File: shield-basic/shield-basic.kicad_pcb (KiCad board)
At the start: 2 copper layers, 0 parts

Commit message: Place the components in the Board. Change some footprint because kicad will remove the library.
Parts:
- added 1pin: VAL**, Connect:1pin, F.Cu at (191.0, 50.0)
- added 1pin: VAL**, Connect:1pin, F.Cu at (132.0, 50.0)
- added 1pin: VAL**, Connect:1pin, F.Cu at (191.0, 117.0)
- added 1pin: VAL**, Connect:1pin, F.Cu at (132.0, 117.0)
- added C1: 18n, Capacitors_SMD:C_0805, F.Cu at (141.0, 57.0)
- added C10: 2.2u, Capacitors_SMD:C_0805, F.Cu at (180.0, 80.0)
- added C11: 10n, Capacitors_SMD:C_0805, F.Cu at (176.0, 88.0)
- added C12: 220u, Capacitors_SMD:c_elec_6.3x7.7, F.Cu at (169.0, 90.0)
- added C13: 100n, Capacitors_SMD:C_0805, F.Cu at (180.0, 88.0)
- added C2: 100nF, Capacitors_SMD:C_0805, F.Cu at (159.0, 57.0)
- added C3: 18n, Capacitors_SMD:C_0805, F.Cu at (165.0, 57.0)
- added C4: 100 nF, Capacitors_SMD:C_0805, F.Cu at (159.0, 68.0)
- added C5: 3.3 uF, Capacitors_SMD:C_0805, F.Cu at (162.0, 68.0)
- added C6: 100 nF, Capacitors_SMD:C_0805, F.Cu at (159.0, 80.0)
- added C7: 47n, Capacitors_SMD:C_0805, F.Cu at (144.0, 88.0)
- added C8: 10 uF, Capacitors_SMD:C_0805, F.Cu at (147.0, 88.0)
- added C9: 100n, Capacitors_SMD:C_0805, F.Cu at (176.0, 80.0)
- added CON1: SD_Card, Connect:SD_Card_Receptacle, B.Cu at (132.0, 69.0)
- added D1: LED_RGB_A, Dreamster:rgb_led_plcc6, F.Cu at (161.0, 112.0)
- added IC1: DRV8833, Housings_SSOP:TSSOP-16_4.4x5mm_Pitch0.65mm, F.Cu at (169.0, 81.0)
- added L1: 1 uH, Capacitors_SMD:C_0805, F.Cu at (156.0, 57.0)
- added L2: 1 uH, Capacitors_SMD:C_0805, F.Cu at (156.0, 68.0)
- added L3: 1 uH, Capacitors_SMD:C_0805, F.Cu at (156.0, 80.0)
- added P1: CONN_01X04, Socket_Strips:Socket_Strip_Straight_1x04, F.Cu at (193.0, 105.0)
- added P2: CONN_01X04, Socket_Strips:Socket_Strip_Straight_1x04, F.Cu at (193.0, 63.0)
- added P3: CONN_01X04, Socket_Strips:Socket_Strip_Straight_1x04, F.Cu at (161.5, 119.5)
- added P4: CONN_01X04, Socket_Strips:Socket_Strip_Straight_1x04, F.Cu at (130.0, 105.0)
- added P5: CONN_01X04, Socket_Strips:Socket_Strip_Straight_1x04, F.Cu at (130.0, 63.0)
- added P6: CONN_01X02, Socket_Strips:Socket_Strip_Straight_1x02, F.Cu at (184.0, 109.0)
- added P7: CONN_01X02, Socket_Strips:Socket_Strip_Straight_1x02, F.Cu at (178.0, 109.0)
- added P8: CONN_01X06, Socket_Strips:Socket_Strip_Straight_1x06, F.Cu at (178.0, 118.0)
- added P9: speaker, Socket_Strips:Socket_Strip_Straight_1x02, F.Cu at (138.0, 112.0)
- added Q1: PNP, Transistors_SMD:sot23, F.Cu at (174.0, 54.0)
- added Q2: NPN, Transistors_SMD:sot23, F.Cu at (157.0, 103.0)
- added R1: 10k, Resistors_SMD:R_0805, F.Cu at (169.0, 114.0)
- added R10: 100, Resistors_SMD:R_0805, F.Cu at (193.0, 71.0)
- added R11: 10k, Resistors_SMD:R_0805, F.Cu at (192.0, 96.0)
- added R12: 10k, Resistors_SMD:R_0805, F.Cu at (161.0, 103.0)
- added R2: 10k, Resistors_SMD:R_0805, F.Cu at (169.0, 111.0)
- added R3: 10k, Resistors_SMD:R_0805, F.Cu at (169.0, 108.0)
- added R4: 2.2k, Resistors_SMD:R_0805, F.Cu at (144.0, 57.0)
- added R5: 2.2k, Resistors_SMD:R_0805, F.Cu at (162.0, 57.0)
- added R6: 10, Resistors_SMD:R_0805, F.Cu at (144.0, 80.0)
- added R7: 100, Resistors_SMD:R_0805, F.Cu at (130.0, 71.0)
- added R8: 100, Resistors_SMD:R_0805, F.Cu at (174.0, 58.0)
- added R9: 10k, Resistors_SMD:R_0805, F.Cu at (131.0, 96.0)
- added RV1: 10k, SMD_Packages:POT_SMD, F.Cu at (147.0, 112.0)
- added RV2: POT, SMD_Packages:POT_SMD, F.Cu at (131.0, 91.0)
- added RV3: POT, SMD_Packages:POT_SMD, F.Cu at (192.0, 91.0)
- added U1: TL082, Housings_SOIC:SOIC-8_3.9x4.9mm_Pitch1.27mm, F.Cu at (150.0, 58.0)
- added U19: TL082, Housings_SOIC:SOIC-8_3.9x4.9mm_Pitch1.27mm, F.Cu at (150.0, 69.0)
- added U2: LM386, Housings_SSOP:MSOP-8_3x3mm_Pitch0.65mm, F.Cu at (150.0, 80.0)
- added U3: TCRT1000, Socket_Strips:Socket_Strip_Angled_1x04, F.Cu at (130.0, 79.0)
- added U4: TCRT1000, Socket_Strips:Socket_Strip_Angled_1x04, F.Cu at (193.0, 79.0)
- added U5: ARDUINO_SHIELD, Dreamster:arduino_shield, F.Cu at (188.0, 47.0)
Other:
- board outline added: 67 x 75 mm

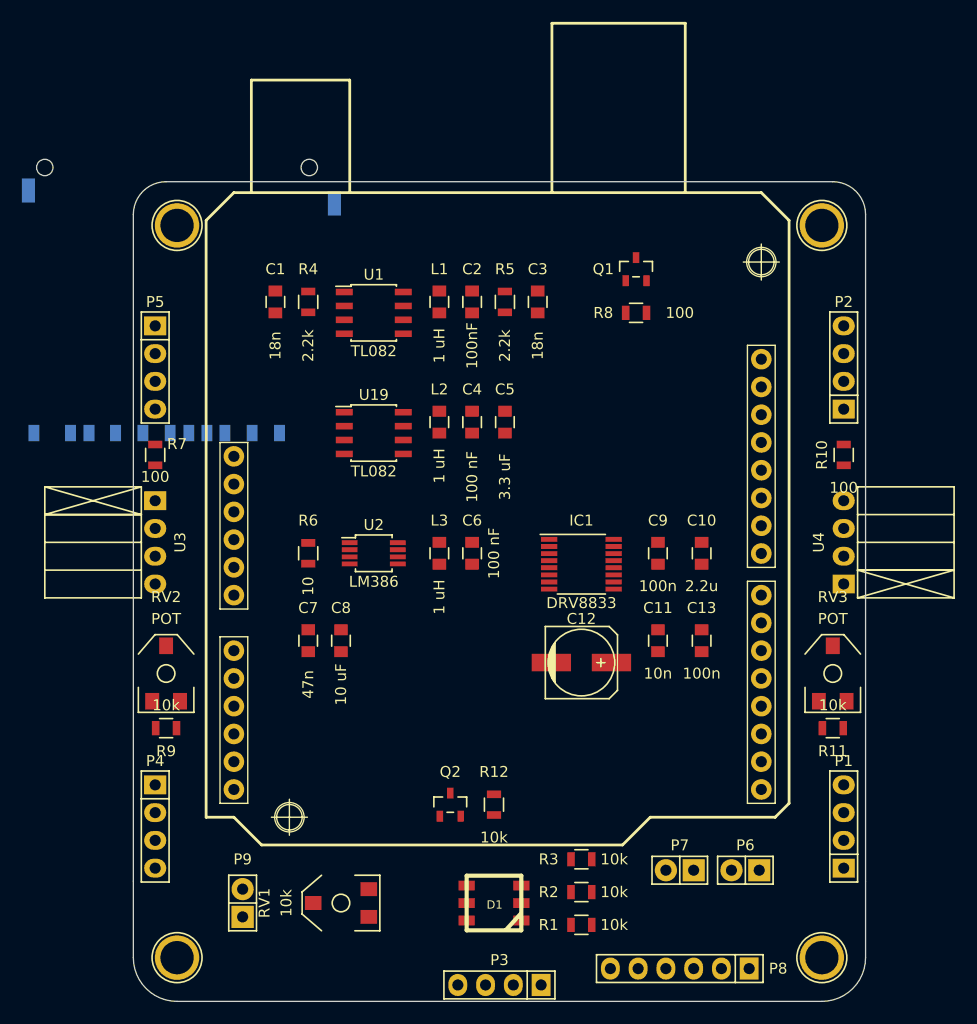
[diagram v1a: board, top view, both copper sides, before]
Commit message: Change the board size
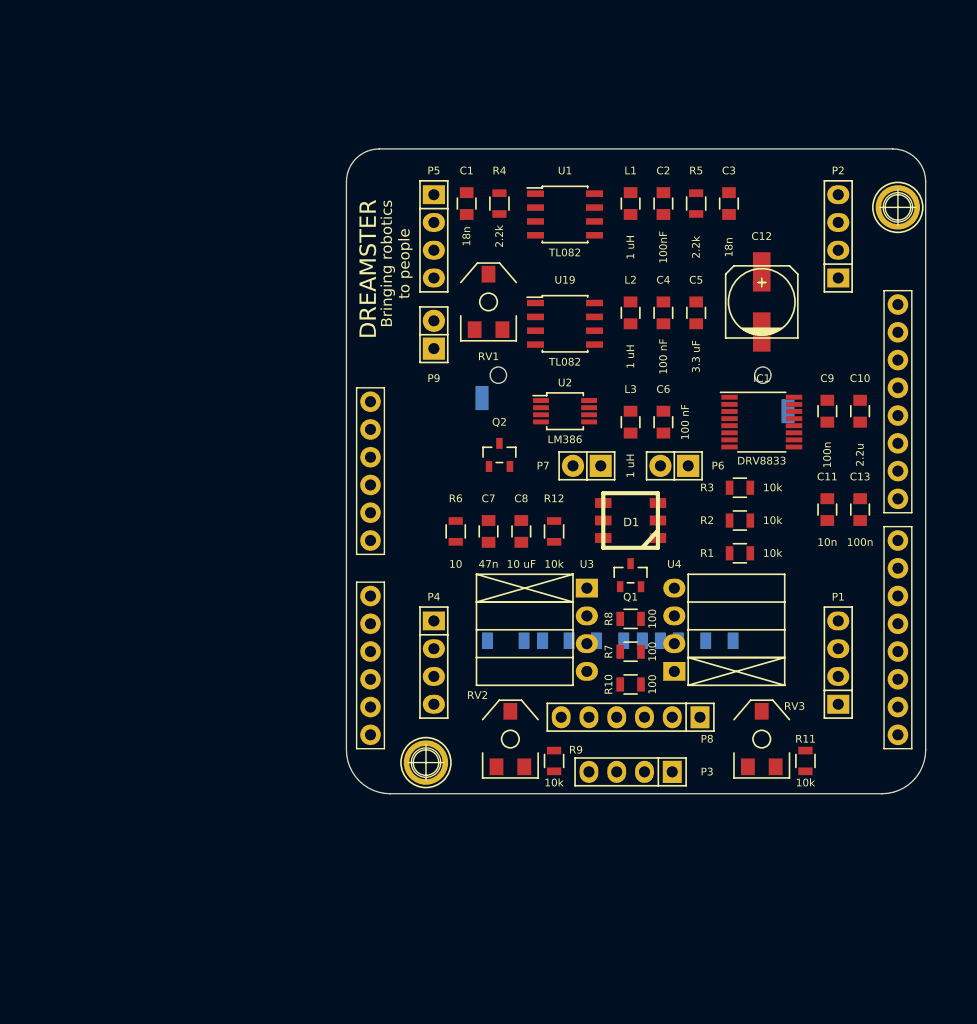
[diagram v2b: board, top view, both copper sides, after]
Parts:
- removed the 1pin at (191.0, 50.0)
- removed the 1pin at (132.0, 117.0)
- moved 1pin 66.0 mm to (197.9, 48.4)
- moved RV1 56.6 mm to (160.5, 57.0), turned to 0 degrees
- moved P9 54.9 mm to (155.5, 60.0)
- moved R7 47.1 mm to (173.5, 89.0), turned to 0 degrees
- moved CON1 45.6 mm to (173.5, 88.0)
- moved 1pin 40.4 mm to (154.8, 99.2)
- moved U3 40.3 mm to (169.5, 87.0)
- moved P7 38.0 mm to (169.5, 72.0)
- moved P6 37.6 mm to (177.5, 72.0)
- moved D1 37.2 mm to (173.5, 77.0)
- moved R1 37.0 mm to (183.5, 80.0)
- moved R2 37.0 mm to (183.5, 77.0)
- moved R3 37.0 mm to (183.5, 74.0)
- moved C12 36.9 mm to (185.5, 57.0), turned to 90 degrees
- moved R9 35.6 mm to (166.5, 99.0), turned to 270 degrees
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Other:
- board size 67 x 75 mm -> 53 x 59 mm
- board text added: "Bringing robotics to people"
- board text added: "DREAMSTER"

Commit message: Added reset buttom.
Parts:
- added C14: 100n, Capacitors_SMD:C_0805, F.Cu at (164.0, 68.0)
- added C15: 100n, Capacitors_SMD:C_0805, F.Cu at (161.0, 68.0)
- added D2: CD1206-S01575, Capacitors_SMD:C_1206, F.Cu at (150.5, 62.0)
- added R13: 10k, Resistors_SMD:R_0805, F.Cu at (154.0, 75.5)
- added SW1: SW_PUSH, Discret:SW_PUSH_SMALL, F.Cu at (155.5, 68.5)
- C2: value 100nF -> 100n
- C4, C6: value 100 nF -> 100n
- C5: value 3.3 uF -> 3.3u
- C8: value 10 uF -> 10u
- L1, L2, L3: value 1 uH -> 1u
- moved Q2 12.5 mm to (154.0, 81.0)
- moved U2 1.50 mm to (169.0, 67.0)
- moved C6 1.41 mm to (177.5, 67.0)
- moved L3 1.41 mm to (174.5, 67.0)
- moved C2 1.00 mm to (177.5, 48.0)
- moved C3 1.00 mm to (183.5, 48.0)
- moved C4 1.00 mm to (177.5, 58.0)
- moved C5 1.00 mm to (180.5, 58.0)
- moved L1 1.00 mm to (174.5, 48.0)
- moved L2 1.00 mm to (174.5, 58.0)
- moved R3 1.00 mm to (183.5, 75.0)
- moved R5 1.00 mm to (180.5, 48.0)
- moved U3 1.00 mm to (168.5, 87.0)
- moved U4 1.00 mm to (178.5, 87.0)
- moved C1 0.50 mm to (159.0, 48.0)
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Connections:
- U5 pad RES: (no net) -> /RESET

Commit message: Correct HCS04 sensor position.
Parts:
- turned P3 to 180 degrees
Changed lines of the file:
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@@
   )
   (module Socket_Strips:Socket_Strip_Straight_1x04 (layer F.Cu)
-    (at 173.5 100)
+    (at 173.5 100 180)
     (descr "Through hole socket strip")
     (tags "socket strip")
-    (fp_text reference P3 (at 6.5 0) (layer F.SilkS)
+    (fp_text reference P3 (at 4.5 2 180) (layer F.SilkS)
       (effects (font (size 0.7 0.7) (thickness 0.125)))
     )
-    (fp_text value CONN_01X04 (at 0 0) (layer F.SilkS) hide
+    (fp_text value CONN_01X04 (at 0 0 180) (layer F.SilkS) hide
       (effects (font (size 0.7 0.7) (thickness 0.125)))
     )
@@
     (fp_line (start 5.08 -1.27) (end 5.08 1.27) (layer F.SilkS) (width 0.15))
     (fp_line (start 5.08 1.27) (end 2.54 1.27) (layer F.SilkS) (width 0.15))
-    (pad 1 thru_hole rect (at 3.81 0 180) (size 1.7272 2.032) (drill 1.016) (layers *.Cu *.Mask F.SilkS)
+    (pad 1 thru_hole rect (at 3.81 0) (size 1.7272 2.032) (drill 1.016) (layers *.Cu *.Mask F.SilkS)
       (net 9 +5VD))
-    (pad 2 thru_hole oval (at 1.27 0 180) (size 1.7272 2.032) (drill 1.016) (layers *.Cu *.Mask F.SilkS)
+    (pad 2 thru_hole oval (at 1.27 0) (size 1.7272 2.032) (drill 1.016) (layers *.Cu *.Mask F.SilkS)
       (net 23 /TRG_A))
-    (pad 3 thru_hole oval (at -1.27 0 180) (size 1.7272 2.032) (drill 1.016) (layers *.Cu *.Mask F.SilkS)
+    (pad 3 thru_hole oval (at -1.27 0) (size 1.7272 2.032) (drill 1.016) (layers *.Cu *.Mask F.SilkS)
       (net 24 /ECHO_A))
-    (pad 4 thru_hole oval (at -3.81 0 180) (size 1.7272 2.032) (drill 1.016) (layers *.Cu *.Mask F.SilkS)
+    (pad 4 thru_hole oval (at -3.81 0) (size 1.7272 2.032) (drill 1.016) (layers *.Cu *.Mask F.SilkS)
       (net 2 GND))
     (model Socket_Strips/Socket_Strip_Straight_1x04.wrl

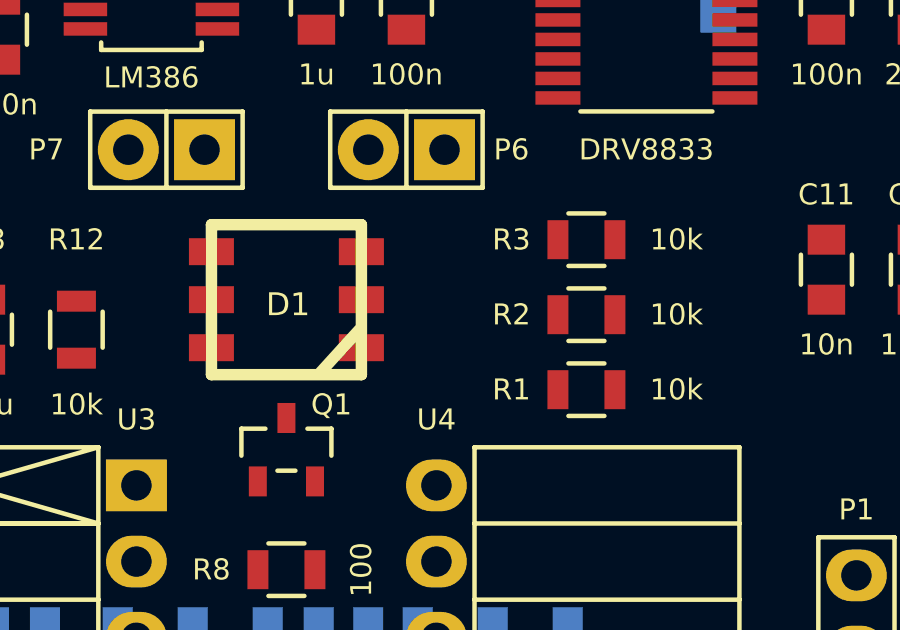
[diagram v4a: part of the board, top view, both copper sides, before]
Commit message: Correct LED RGB position.
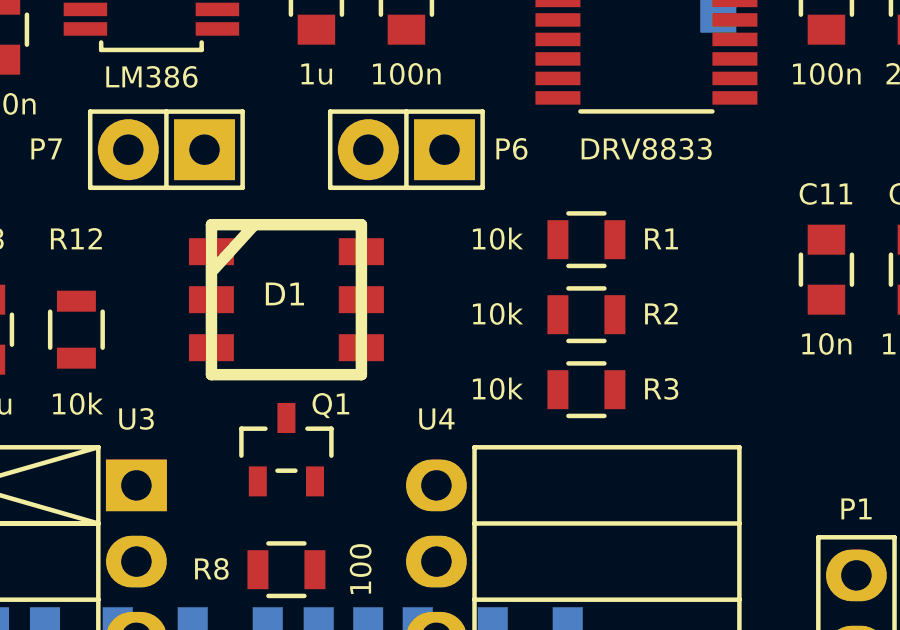
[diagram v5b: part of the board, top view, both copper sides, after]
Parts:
- moved R1 5.00 mm to (183.5, 75.0), turned to 180 degrees
- moved R3 5.00 mm to (183.5, 80.0), turned to 180 degrees
- turned D1 to 180 degrees
- turned R2 to 180 degrees
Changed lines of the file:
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@@
     (links 141)
     (no_connects 141)
-    (area 147.449999 42.949999 200.550001 102.050001)
+    (area 143.790048 41.496 201.004 105.299833)
     (thickness 1.6)
     (drawings 10)
@@
     (add_net "Net-(RV1-Pad2)")
   )
+  (module Dreamster:rgb_led_plcc6 (layer F.Cu)
+    (at 173.5 77 180)
+    (fp_text reference D1 (at 0.05334 0.16256 180) (layer F.SilkS)
+      (effects (font (size 0.762 0.762) (thickness 0.127)))
+    )
+    (fp_text value LED_RGB_A (at 0 3.429 180) (layer F.SilkS) hide
+      (effects (font (size 0.762 0.762) (thickness 0.127)))
+    )
+    (fp_line (start 1.143 2.413) (end 2.413 1.016) (layer F.SilkS) (width 0.381))
+    (fp_line (start -2.49936 2.49936) (end -2.49936 -2.49936) (layer F.SilkS) (width 0.381))
+    (fp_line (start -2.49936 -2.49936) (end 2.49936 -2.49936) (layer F.SilkS) (width 0.381))
+    (fp_line (start 2.49936 -2.49936) (end 2.49936 2.49936) (layer F.SilkS) (width 0.381))
+    (fp_line (start 2.49936 2.49936) (end -2.49936 2.49936) (layer F.SilkS) (width 0.381))
+    (pad 4 smd rect (at -2.49936 -1.6002 270) (size 0.89916 1.50114) (layers F.Cu F.Paste F.Mask)
+      (net 18 "Net-(D1-Pad4)"))
+    (pad 5 smd rect (at -2.49936 0 270) (size 0.89916 1.50114) (layers F.Cu F.Paste F.Mask)
+      (net 16 "Net-(D1-Pad5)"))
+    (pad 6 smd rect (at -2.49936 1.6002 270) (size 0.89916 1.50114) (layers F.Cu F.Paste F.Mask)
+      (net 17 "Net-(D1-Pad6)"))
+    (pad 1 smd rect (at 2.49936 1.6002 270) (size 0.89916 1.50114) (layers F.Cu F.Paste F.Mask)
+      (net 15 "Net-(D1-Pad1)"))
+    (pad 2 smd rect (at 2.49936 0 270) (size 0.89916 1.50114) (layers F.Cu F.Paste F.Mask)
+      (net 15 "Net-(D1-Pad1)"))
+    (pad 3 smd rect (at 2.49936 -1.6002 270) (size 0.89916 1.50114) (layers F.Cu F.Paste F.Mask)
+      (net 15 "Net-(D1-Pad1)"))
+  )
   (module Connect:1pin (layer F.Cu)
     (at 154.775 99.15)
@@
     (pad "" np_thru_hole circle (at -12.1 -24.3) (size 1.5 1.5) (drill 1.5) (layers *.Cu *.Mask B.SilkS))
   )
-  (module Dreamster:rgb_led_plcc6 (layer F.Cu)
-    (at 173.5 77)
-    (fp_text reference D1 (at 0.05334 0.16256) (layer F.SilkS)
-      (effects (font (size 0.762 0.762) (thickness 0.127)))
-    )
-    (fp_text value LED_RGB_A (at 0 3.429) (layer F.SilkS) hide
-      (effects (font (size 0.762 0.762) (thickness 0.127)))
-    )
-    (fp_line (start 1.143 2.413) (end 2.413 1.016) (layer F.SilkS) (width 0.381))
-    (fp_line (start -2.49936 2.49936) (end -2.49936 -2.49936) (layer F.SilkS) (width 0.381))
-    (fp_line (start -2.49936 -2.49936) (end 2.49936 -2.49936) (layer F.SilkS) (width 0.381))
-    (fp_line (start 2.49936 -2.49936) (end 2.49936 2.49936) (layer F.SilkS) (width 0.381))
-    (fp_line (start 2.49936 2.49936) (end -2.49936 2.49936) (layer F.SilkS) (width 0.381))
-    (pad 1 smd rect (at -2.49936 -1.6002 90) (size 0.89916 1.50114) (layers F.Cu F.Paste F.Mask)
-      (net 15 "Net-(D1-Pad1)"))
-    (pad 3 smd rect (at -2.49936 0 90) (size 0.89916 1.50114) (layers F.Cu F.Paste F.Mask)
-      (net 15 "Net-(D1-Pad1)"))
-    (pad 5 smd rect (at -2.49936 1.6002 90) (size 0.89916 1.50114) (layers F.Cu F.Paste F.Mask)
-      (net 16 "Net-(D1-Pad5)"))
-    (pad 6 smd rect (at 2.49936 1.6002 90) (size 0.89916 1.50114) (layers F.Cu F.Paste F.Mask)
-      (net 17 "Net-(D1-Pad6)"))
-    (pad 4 smd rect (at 2.49936 0 90) (size 0.89916 1.50114) (layers F.Cu F.Paste F.Mask)
-      (net 18 "Net-(D1-Pad4)"))
-    (pad 2 smd rect (at 2.49936 -1.6002 90) (size 0.89916 1.50114) (layers F.Cu F.Paste F.Mask)
-      (net 15 "Net-(D1-Pad1)"))
-  )
   (module Socket_Strips:Socket_Strip_Straight_1x04 (layer F.Cu)
     (at 192.5 90 270)
@@
   )
   (module Resistors_SMD:R_0805 (layer F.Cu)
-    (at 183.5 80)
+    (at 183.5 75 180)
     (descr "Resistor SMD 0805, reflow soldering, Vishay (see dcrcw.pdf)")
     (tags "resistor 0805")
     (attr smd)
-    (fp_text reference R1 (at -2.5 0) (layer F.SilkS)
-      (effects (font (size 0.7 0.7) (thickness 0.125)))
-    )
-    (fp_text value 10k (at 3 0) (layer F.SilkS)
+    (fp_text reference R1 (at -2.5 0 180) (layer F.SilkS)
+      (effects (font (size 0.7 0.7) (thickness 0.125)))
+    )
+    (fp_text value 10k (at 3 0 180) (layer F.SilkS)
       (effects (font (size 0.7 0.7) (thickness 0.125)))
     )
@@
     (fp_line (start 0.6 0.875) (end -0.6 0.875) (layer F.SilkS) (width 0.15))
     (fp_line (start -0.6 -0.875) (end 0.6 -0.875) (layer F.SilkS) (width 0.15))
-    (pad 1 smd rect (at -0.95 0) (size 0.7 1.3) (layers F.Cu F.Paste F.Mask)
+    (pad 1 smd rect (at -0.95 0 180) (size 0.7 1.3) (layers F.Cu F.Paste F.Mask)
       (net 14 /RED))
-    (pad 2 smd rect (at 0.95 0) (size 0.7 1.3) (layers F.Cu F.Paste F.Mask)
+    (pad 2 smd rect (at 0.95 0 180) (size 0.7 1.3) (layers F.Cu F.Paste F.Mask)
       (net 17 "Net-(D1-Pad6)"))
     (model Resistors_SMD/R_0805.wrl
@@
   )
   (module Resistors_SMD:R_0805 (layer F.Cu)
-    (at 183.5 77.5)
+    (at 183.5 77.5 180)
     (descr "Resistor SMD 0805, reflow soldering, Vishay (see dcrcw.pdf)")
     (tags "resistor 0805")
     (attr smd)
-    (fp_text reference R2 (at -2.5 0) (layer F.SilkS)
-      (effects (font (size 0.7 0.7) (thickness 0.125)))
-    )
-    (fp_text value 10k (at 3 0) (layer F.SilkS)
+    (fp_text reference R2 (at -2.5 0 180) (layer F.SilkS)
+      (effects (font (size 0.7 0.7) (thickness 0.125)))
+    )
+    (fp_text value 10k (at 3 0 180) (layer F.SilkS)
       (effects (font (size 0.7 0.7) (thickness 0.125)))
     )
@@
     (fp_line (start 0.6 0.875) (end -0.6 0.875) (layer F.SilkS) (width 0.15))
     (fp_line (start -0.6 -0.875) (end 0.6 -0.875) (layer F.SilkS) (width 0.15))
-    (pad 1 smd rect (at -0.95 0) (size 0.7 1.3) (layers F.Cu F.Paste F.Mask)
+    (pad 1 smd rect (at -0.95 0 180) (size 0.7 1.3) (layers F.Cu F.Paste F.Mask)
       (net 11 /GREEN))
-    (pad 2 smd rect (at 0.95 0) (size 0.7 1.3) (layers F.Cu F.Paste F.Mask)
+    (pad 2 smd rect (at 0.95 0 180) (size 0.7 1.3) (layers F.Cu F.Paste F.Mask)
       (net 16 "Net-(D1-Pad5)"))
     (model Resistors_SMD/R_0805.wrl
@@
   )
   (module Resistors_SMD:R_0805 (layer F.Cu)
-    (at 183.5 75)
+    (at 183.5 80 180)
     (descr "Resistor SMD 0805, reflow soldering, Vishay (see dcrcw.pdf)")
     (tags "resistor 0805")
     (attr smd)
-    (fp_text reference R3 (at -2.5 0) (layer F.SilkS)
-      (effects (font (size 0.7 0.7) (thickness 0.125)))
-    )
-    (fp_text value 10k (at 3 0) (layer F.SilkS)
+    (fp_text reference R3 (at -2.5 0 180) (layer F.SilkS)
+      (effects (font (size 0.7 0.7) (thickness 0.125)))
+    )
+    (fp_text value 10k (at 3 0 180) (layer F.SilkS)
       (effects (font (size 0.7 0.7) (thickness 0.125)))
     )
@@
     (fp_line (start 0.6 0.875) (end -0.6 0.875) (layer F.SilkS) (width 0.15))
     (fp_line (start -0.6 -0.875) (end 0.6 -0.875) (layer F.SilkS) (width 0.15))
-    (pad 1 smd rect (at -0.95 0) (size 0.7 1.3) (layers F.Cu F.Paste F.Mask)
+    (pad 1 smd rect (at -0.95 0 180) (size 0.7 1.3) (layers F.Cu F.Paste F.Mask)
       (net 13 /BLUE))
-    (pad 2 smd rect (at 0.95 0) (size 0.7 1.3) (layers F.Cu F.Paste F.Mask)
+    (pad 2 smd rect (at 0.95 0 180) (size 0.7 1.3) (layers F.Cu F.Paste F.Mask)
       (net 18 "Net-(D1-Pad4)"))
     (model Resistors_SMD/R_0805.wrl

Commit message: PCB routed.
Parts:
- moved P7 23.3 mm to (192.5, 68.5), turned to 90 degrees
- moved P6 18.3 mm to (192.5, 61.5), turned to 90 degrees
- moved C10 17.5 mm to (177.5, 71.0)
- moved C9 17.5 mm to (174.5, 71.0)
- moved U3 6.80 mm to (163.0, 91.0), turned to 0 degrees
- moved U4 6.73 mm to (183.5, 91.5), turned to 0 degrees
- moved C6 2.50 mm to (177.5, 64.5)
- moved L3 2.50 mm to (174.5, 64.5)
- moved IC1 1.58 mm to (185.0, 66.5)
- moved CON1 1.41 mm to (174.5, 87.0)
- moved U2 1.12 mm to (169.5, 68.0)
- moved C12 1.00 mm to (186.0, 56.0)
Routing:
- net GND: track 0.00 -> 338.9 mm
- net +5VD: track 0.00 -> 277.6 mm
- net /TRG_C: track 0.00 -> 97.0 mm
- net /ECHO_B: track 0.00 -> 91.2 mm
- net /hbridge/RMI1: track 0.00 -> 68.4 mm
- net /TRG_B: track 0.00 -> 67.1 mm, vias 0 -> 1
- net /hbridge/LMI2: track 0.00 -> 64.1 mm, vias 0 -> 1
- net /ECHO_C: track 0.00 -> 64.0 mm, vias 0 -> 1
- net /sound/In: track 0.00 -> 62.1 mm, vias 0 -> 1
- net /hbridge/RMI2: track 0.00 -> 58.1 mm
- net /hbridge/LMI1: track 0.00 -> 55.7 mm, vias 0 -> 1
- net /RED: track 0.00 -> 51.3 mm, vias 0 -> 2
- net /BLUE: track 0.00 -> 50.4 mm, vias 0 -> 2
- net /ECHO_A: track 0.00 -> 50.0 mm
- net /irsensor/RSENS: track 0.00 -> 46.5 mm
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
